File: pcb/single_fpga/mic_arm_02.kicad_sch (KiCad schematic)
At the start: 17 parts, among them U102 CDCLVC1108PW, U17 IM72D128V01XTMA1, U18 IM72D128V01XTMA1, U19 IM72D128V01XTMA1, U20 IM72D128V01XTMA1, U21 IM72D128V01XTMA1, U22 IM72D128V01XTMA1, U23 IM72D128V01XTMA1, U24 IM72D128V01XTMA1

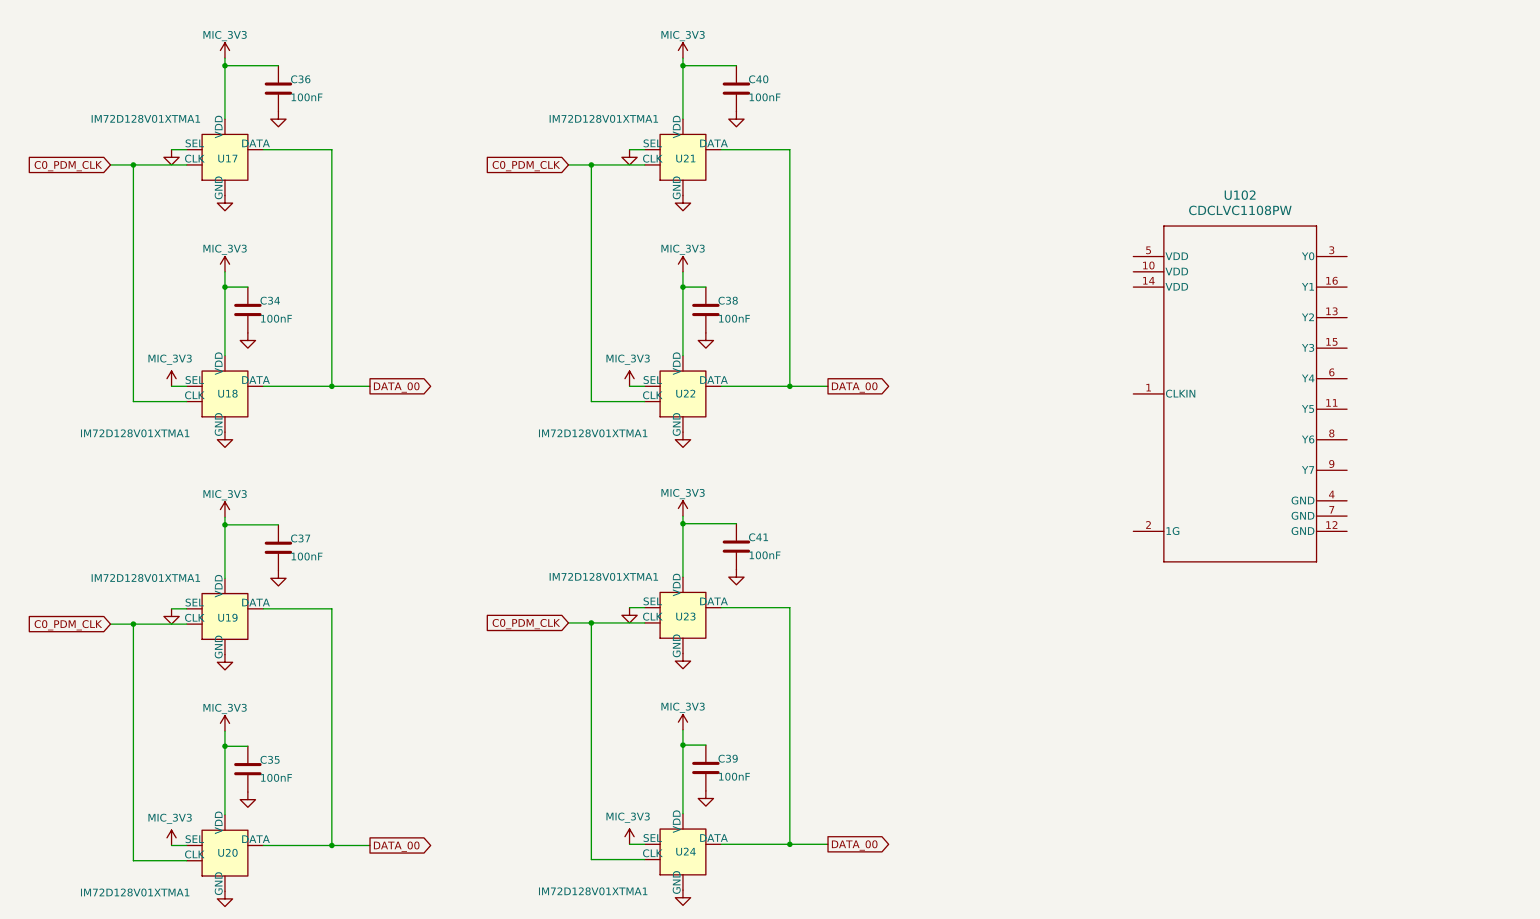
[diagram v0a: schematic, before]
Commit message: Fixed clocks and names.
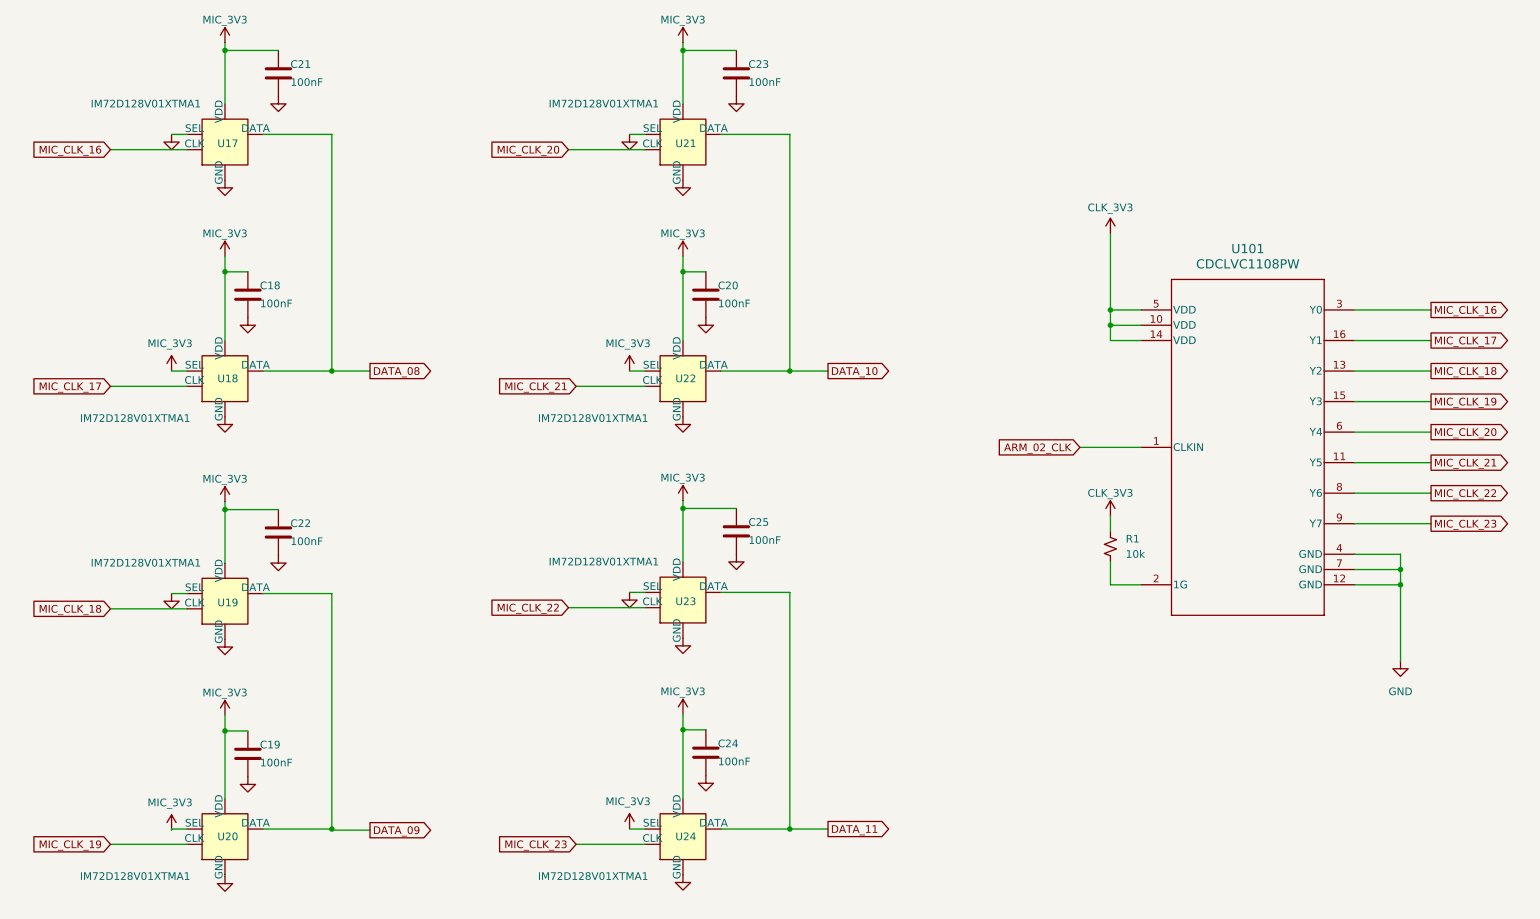
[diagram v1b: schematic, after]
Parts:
- removed C34, C35, C36, C37, C38, C39, C40, C41: 100nF, Capacitor_SMD:C_0603_1608Metric, symbol Device:C
- removed U102: CDCLVC1108PW, PW0016A_N, symbol CDCLVC1108:CDCLVC1108PW
- added C18, C19, C20, C21, C22, C23, C24, C25: 100nF, Capacitor_SMD:C_0603_1608Metric, symbol Device:C
- added R1: 10k, PCM_SparkFun-Resistor:R_0603_1608Metric, symbol PCM_SparkFun-Resistor:10k_0603
- added U101: CDCLVC1108PW, PW0016A_N, symbol CDCLVC1108:CDCLVC1108PW
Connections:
- net GND: now also C18.2, C19.2, C20.2, C21.2, C22.2, C23.2, C24.2, C25.2, U101.12 (GND), U101.4 (GND), U101.7 (GND)
- net MIC_3V3: now also C18.1, C19.1, C20.1, C21.1, C22.1, C23.1, C24.1, C25.1
- removed net C0_PDM_CLK: U17.3 (CLK), U18.3 (CLK), U19.3 (CLK), U20.3 (CLK), U21.3 (CLK), U22.3 (CLK), U23.3 (CLK), U24.3 (CLK)
- removed net DATA_00: U17.1 (DATA), U18.1 (DATA), U19.1 (DATA), U20.1 (DATA), U21.1 (DATA), U22.1 (DATA), U23.1 (DATA), U24.1 (DATA)
- new net: R1.1, U101.2 (1G)
- new net ARM_02_CLK: U101.1 (CLKIN)
- new net CLK_3V3: R1.2, U101.10 (VDD), U101.14 (VDD), U101.5 (VDD)
- new net DATA_08: U17.1 (DATA), U18.1 (DATA)
- new net DATA_09: U19.1 (DATA), U20.1 (DATA)
- new net DATA_10: U21.1 (DATA), U22.1 (DATA)
- new net DATA_11: U23.1 (DATA), U24.1 (DATA)
- new net MIC_CLK_16: U101.3 (Y0), U17.3 (CLK)
- new net MIC_CLK_17: U101.16 (Y1), U18.3 (CLK)
- new net MIC_CLK_18: U101.13 (Y2), U19.3 (CLK)
- new net MIC_CLK_19: U101.15 (Y3), U20.3 (CLK)
- new net MIC_CLK_20: U101.6 (Y4), U21.3 (CLK)
- new net MIC_CLK_21: U101.11 (Y5), U22.3 (CLK)
- new net MIC_CLK_22: U101.8 (Y6), U23.3 (CLK)
- new net MIC_CLK_23: U101.9 (Y7), U24.3 (CLK)

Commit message: Fixed all duplicate refdes's.
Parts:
- renumbered C18 to C34, C19 to C35, C20 to C36, C21 to C37, C22 to C38, C23 to C39, C24 to C40, C25 to C41, R1 to R7

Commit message: Fixed symbol library references.
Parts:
- U101: footprint PW0016A_N -> CDCLVC1108:PW0016A_N
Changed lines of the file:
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@@
 			)
 		)
-		(property "Footprint" "PW0016A_N"
+		(property "Footprint" "CDCLVC1108:PW0016A_N"
 			(at 229.87 95.25 0)
 			(hide yes)

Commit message: Fixed footprints. Added missing mic. Relinked placed footprints.
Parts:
- U17, U18, U19, U20, U21, U22, U23, U24: footprint (none) -> IM72D128:IFX-PG-LLGA-5-4
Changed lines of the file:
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@@
 			)
 		)
-		(property "Footprint" ""
+		(property "Footprint" "IM72D128:IFX-PG-LLGA-5-4"
 			(at 59.69 160.02 0)
 			(hide yes)
@@
 			)
 		)
-		(property "Footprint" ""
+		(property "Footprint" "IM72D128:IFX-PG-LLGA-5-4"
 			(at 135.89 160.02 0)
 			(hide yes)
@@
 			)
 		)
-		(property "Footprint" ""
+		(property "Footprint" "IM72D128:IFX-PG-LLGA-5-4"
 			(at 59.69 83.82 0)
 			(hide yes)
@@
 			)
 		)
-		(property "Footprint" ""
+		(property "Footprint" "IM72D128:IFX-PG-LLGA-5-4"
 			(at 59.69 120.65 0)
 			(hide yes)
@@
 			)
 		)
-		(property "Footprint" ""
+		(property "Footprint" "IM72D128:IFX-PG-LLGA-5-4"
 			(at 59.69 44.45 0)
 			(hide yes)
@@
 			)
 		)
-		(property "Footprint" ""
+		(property "Footprint" "IM72D128:IFX-PG-LLGA-5-4"
 			(at 135.89 83.82 0)
 			(hide yes)
@@
 			)
 		)
-		(property "Footprint" ""
+		(property "Footprint" "IM72D128:IFX-PG-LLGA-5-4"
 			(at 135.89 44.45 0)
 			(hide yes)
@@
 			)
 		)
-		(property "Footprint" ""
+		(property "Footprint" "IM72D128:IFX-PG-LLGA-5-4"
 			(at 135.89 120.65 0)
 			(hide yes)

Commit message: Updated all refdes's.
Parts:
- removed C34, C35, C36, C37, C38, C39, C40, C41: 100nF, Capacitor_SMD:C_0603_1608Metric, symbol Device:C
- removed R7: 10k, PCM_SparkFun-Resistor:R_0603_1608Metric, symbol PCM_SparkFun-Resistor:10k_0603
- removed U101: CDCLVC1108PW, CDCLVC1108:PW0016A_N, symbol CDCLVC1108:CDCLVC1108PW
- removed U17, U18: IM72D128V01XTMA1, IM72D128:IFX-PG-LLGA-5-4, symbol multi_fpga:IM72D128
- added C17, C18, C19, C20, C21, C22, C23, C24: 100nF, Capacitor_SMD:C_0603_1608Metric, symbol Device:C
- added R3: 10k, PCM_SparkFun-Resistor:R_0603_1608Metric, symbol PCM_SparkFun-Resistor:10k_0603
- added U25, U26: IM72D128V01XTMA1, IM72D128:IFX-PG-LLGA-5-4, symbol multi_fpga:IM72D128
- added U27: CDCLVC1108PW, CDCLVC1108:PW0016A_N, symbol CDCLVC1108:CDCLVC1108PW
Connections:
- net ARM_02_CLK: now also U27.1 (CLKIN)
- net CLK_3V3: now also R3.2, U27.10 (VDD), U27.14 (VDD), U27.5 (VDD)
- net DATA_08: now also U19.1 (DATA), U20.1 (DATA)
- net DATA_09: now also U21.1 (DATA), U22.1 (DATA); no longer U19.1 (DATA), U20.1 (DATA)
- net DATA_10: now also U23.1 (DATA), U24.1 (DATA); no longer U21.1 (DATA), U22.1 (DATA)
- net DATA_11: now also U25.1 (DATA), U26.1 (DATA); no longer U23.1 (DATA), U24.1 (DATA)
- net GND: now also C17.2, C18.2, C19.2, C20.2, C21.2, C22.2, C23.2, C24.2, U25.4 (SEL), U25.5 (GND), U26.5 (GND), U27.12 (GND), U27.4 (GND), U27.7 (GND)
- net MIC_3V3: now also C17.1, C18.1, C19.1, C20.1, C21.1, C22.1, C23.1, C24.1, U25.2 (VDD), U26.2 (VDD), U26.4 (SEL)
- net MIC_CLK_16: now also U19.3 (CLK), U27.3 (Y0)
- net MIC_CLK_17: now also U20.3 (CLK), U27.16 (Y1)
- net MIC_CLK_18: now also U21.3 (CLK), U27.13 (Y2); no longer U19.3 (CLK)
- net MIC_CLK_19: now also U22.3 (CLK), U27.15 (Y3); no longer U20.3 (CLK)
- net MIC_CLK_20: now also U23.3 (CLK), U27.6 (Y4); no longer U21.3 (CLK)
- net MIC_CLK_21: now also U24.3 (CLK), U27.11 (Y5); no longer U22.3 (CLK)
- net MIC_CLK_22: now also U25.3 (CLK), U27.8 (Y6); no longer U23.3 (CLK)
- net MIC_CLK_23: now also U26.3 (CLK), U27.9 (Y7); no longer U24.3 (CLK)
- new net: R3.1, U27.2 (1G)
